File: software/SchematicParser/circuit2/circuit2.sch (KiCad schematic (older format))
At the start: 8 parts, among them Q1 Transistor, U1-8 8pinChip

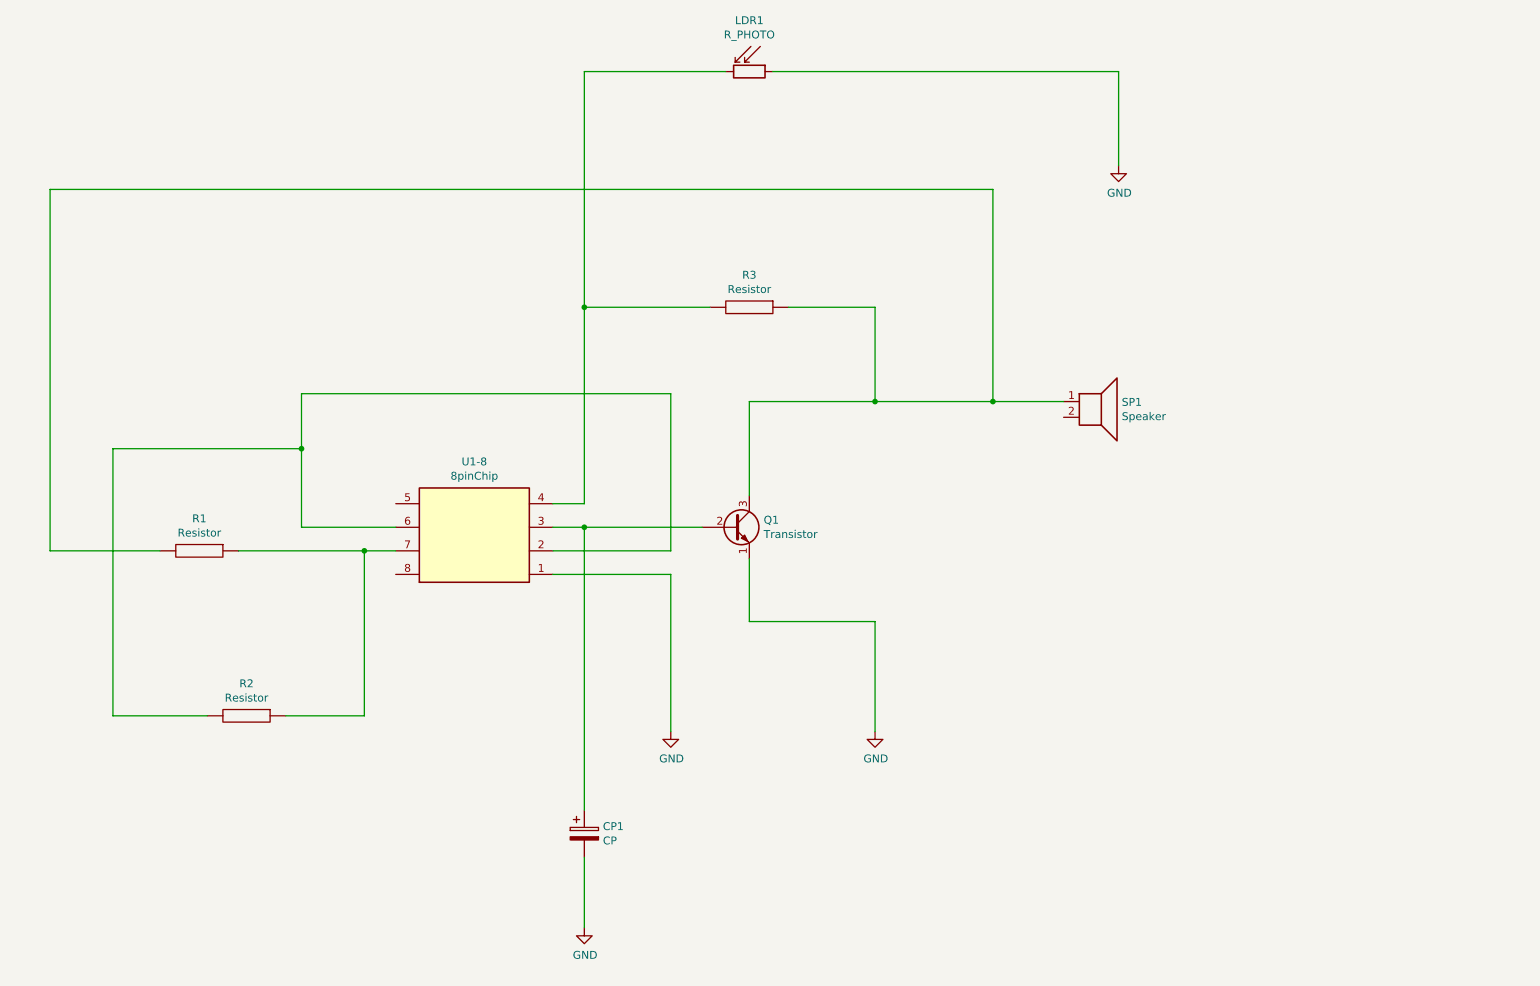
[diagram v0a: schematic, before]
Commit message: modify scale of prefabs
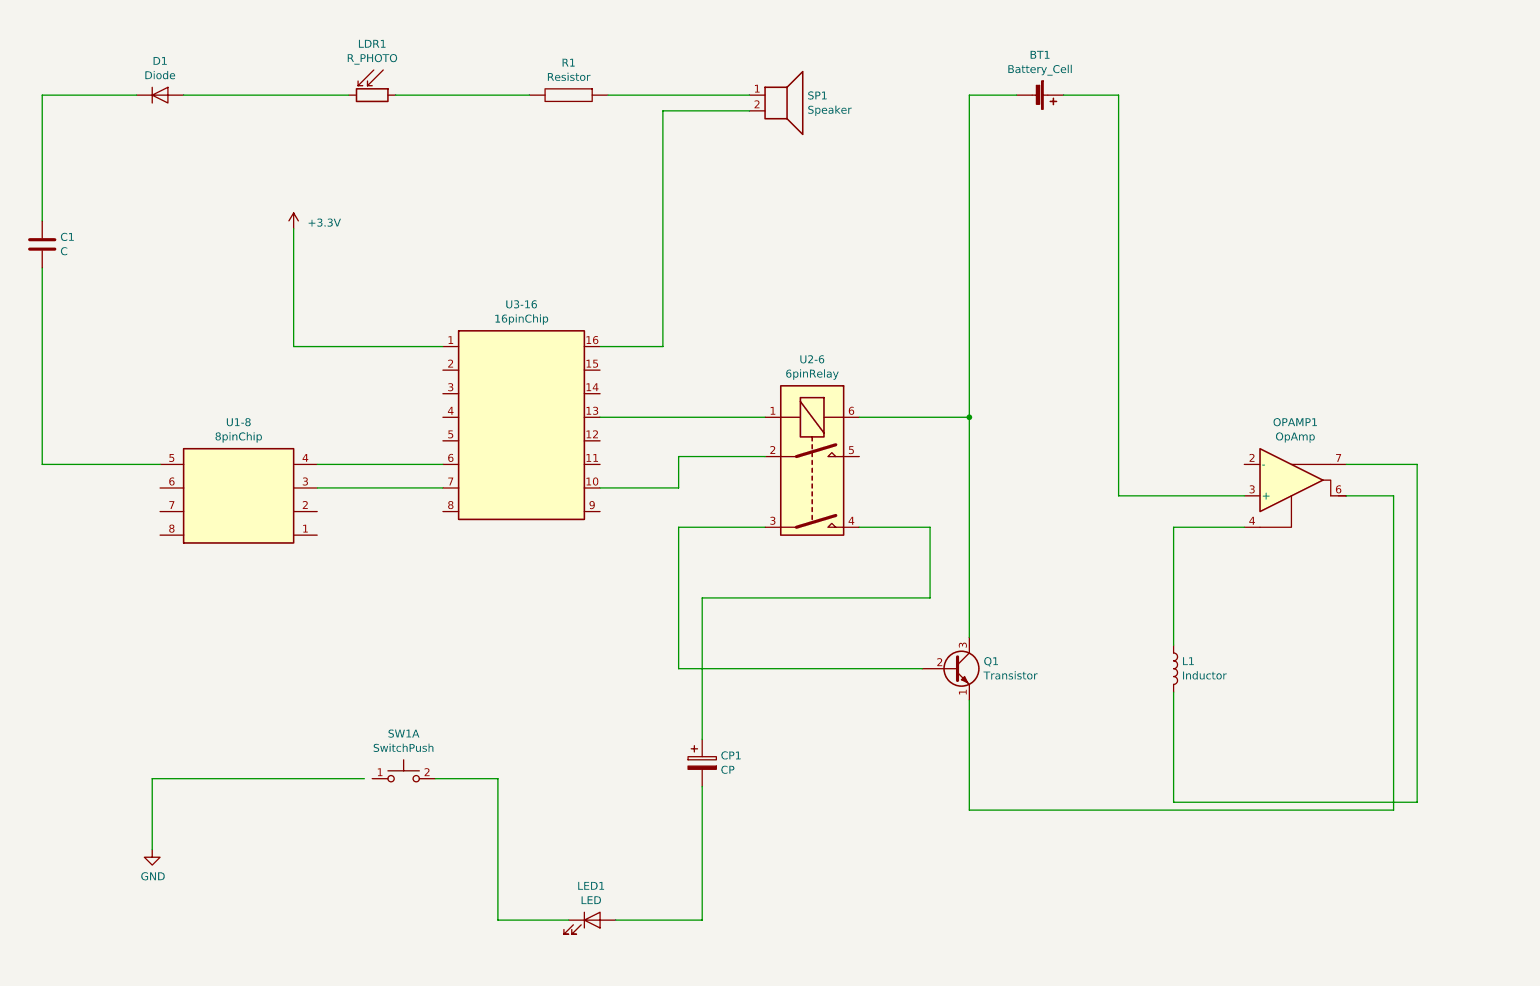
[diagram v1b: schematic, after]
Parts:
- removed R1, R2: Resistor, symbol SchemaBoard_Library:Resistor
- added BT1: Battery_Cell, symbol SchemaBoard_Library:Battery_Cell
- added C1: C, symbol SchemaBoard_Library:C
- added D1: Diode, symbol SchemaBoard_Library:Diode
- added GND1: GND, symbol SchemaBoard_Library:GND
- added L1: Inductor, symbol SchemaBoard_Library:Inductor
- added LED1: LED, symbol SchemaBoard_Library:LED
- added OPAMP1: OpAmp, symbol SchemaBoard_Library:OpAmp
- added PWR1: +3.3V, symbol SchemaBoard_Library:+3.3V
- added SW1: SwitchPush, symbol SchemaBoard_Library:SwitchPush
- added U2-6: 6pinRelay, Relay_THT, symbol SchemaBoard_Library:6pinRelay
- added U3-16: 16pinChip, symbol SchemaBoard_Library:16pinChip
- renumbered R3 to R1
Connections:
- net GND: now also GND1.1 (GND); no longer CP1.2, LDR1.1, Q1.1 (E), U1-8.1
- net at U1-8.2: no longer U1-8.6
- net at U1-8.5: now also C1.2
- net at R1.1, SP1.1: no longer Q1.3 (C)
- net at SP1.2: now also U3-16.16
- new net: U1-8.3, U3-16.7
- new net: U1-8.4, U3-16.6
- new net: LDR1.1, R1.2
- new net: D1.2 (A), LDR1.2
- new net: OPAMP1.6, Q1.1 (E)
- new net: Q1.2 (B), U2-6.3
- new net: BT1.2 (-), Q1.3 (C), U2-6.6
- new net: U2-6.1, U3-16.13
- new net: U2-6.2, U3-16.10
- new net: CP1.1, U2-6.4
- new net: C1.1, D1.1 (K)
- new net: L1.1, OPAMP1.4
- new net: L1.2, OPAMP1.7
- new net: LED1.1 (K), SW1.2 (D)
- new net: CP1.2, LED1.2 (A)
- new net: BT1.1 (+), OPAMP1.3 (+)
- new net +3V3: PWR1.1 (+3V3), U3-16.1
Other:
- moved on the sheet: CP1, LDR1, Q1, R1, SP1, U1-8

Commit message: Bugfix solved the touch problem of profabs
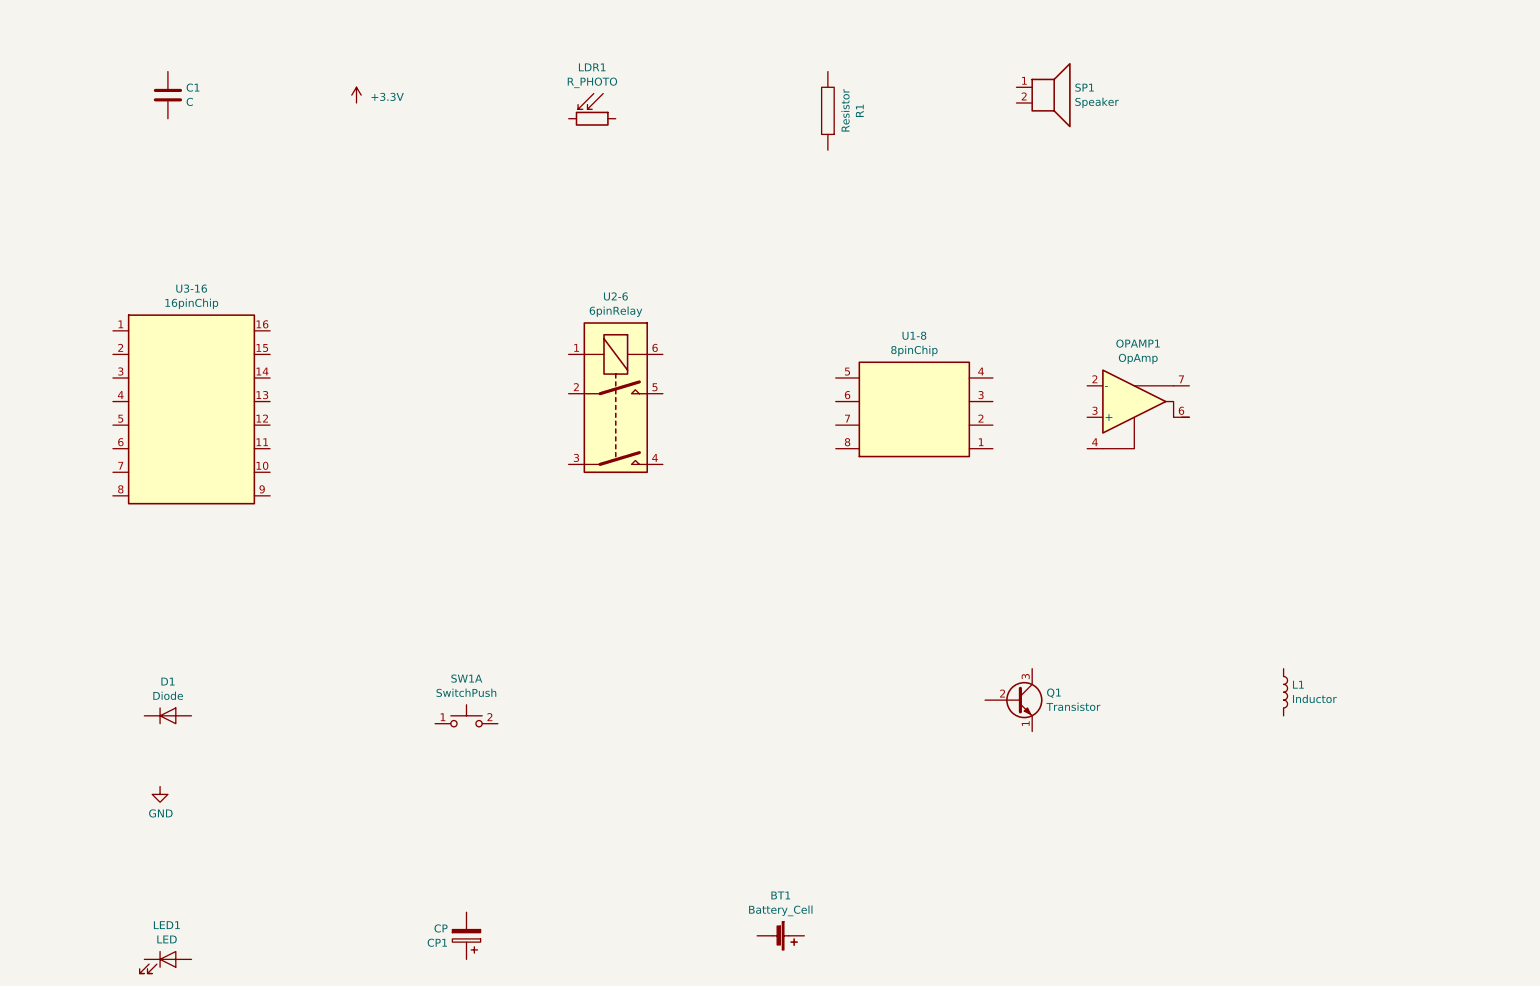
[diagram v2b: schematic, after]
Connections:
- net +3V3: no longer U3-16.1
- net at U1-8.3: no longer U3-16.7
- net at U1-8.4: no longer U3-16.6
- net at U1-8.5: no longer C1.2
- net at SP1.1: no longer R1.1
- net at SP1.2: no longer U3-16.16
- net at LDR1.1: no longer R1.2
- net at LDR1.2: no longer D1.2 (A)
- net at Q1.1 (E): no longer OPAMP1.6
- net at Q1.2 (B): no longer U2-6.3
- net at U2-6.1: no longer U3-16.13
- net at U2-6.2: no longer U3-16.10
- net at U2-6.4: no longer CP1.1
- net at C1.1: no longer D1.1 (K)
- net at L1.1: no longer OPAMP1.4
- net at L1.2: no longer OPAMP1.7
- net at LED1.1 (K): no longer SW1.2 (D)
- net at LED1.2 (A): no longer CP1.2
- net at OPAMP1.3 (+): no longer BT1.1 (+)
- now unconnected: BT1.2 (-), Q1.3 (C), U2-6.6
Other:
- moved on the sheet: BT1, C1, CP1, D1, L1, LDR1, LED1, OPAMP1, Q1, R1, SP1, SW1A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

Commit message: Bugfix remove space when split string into string[]
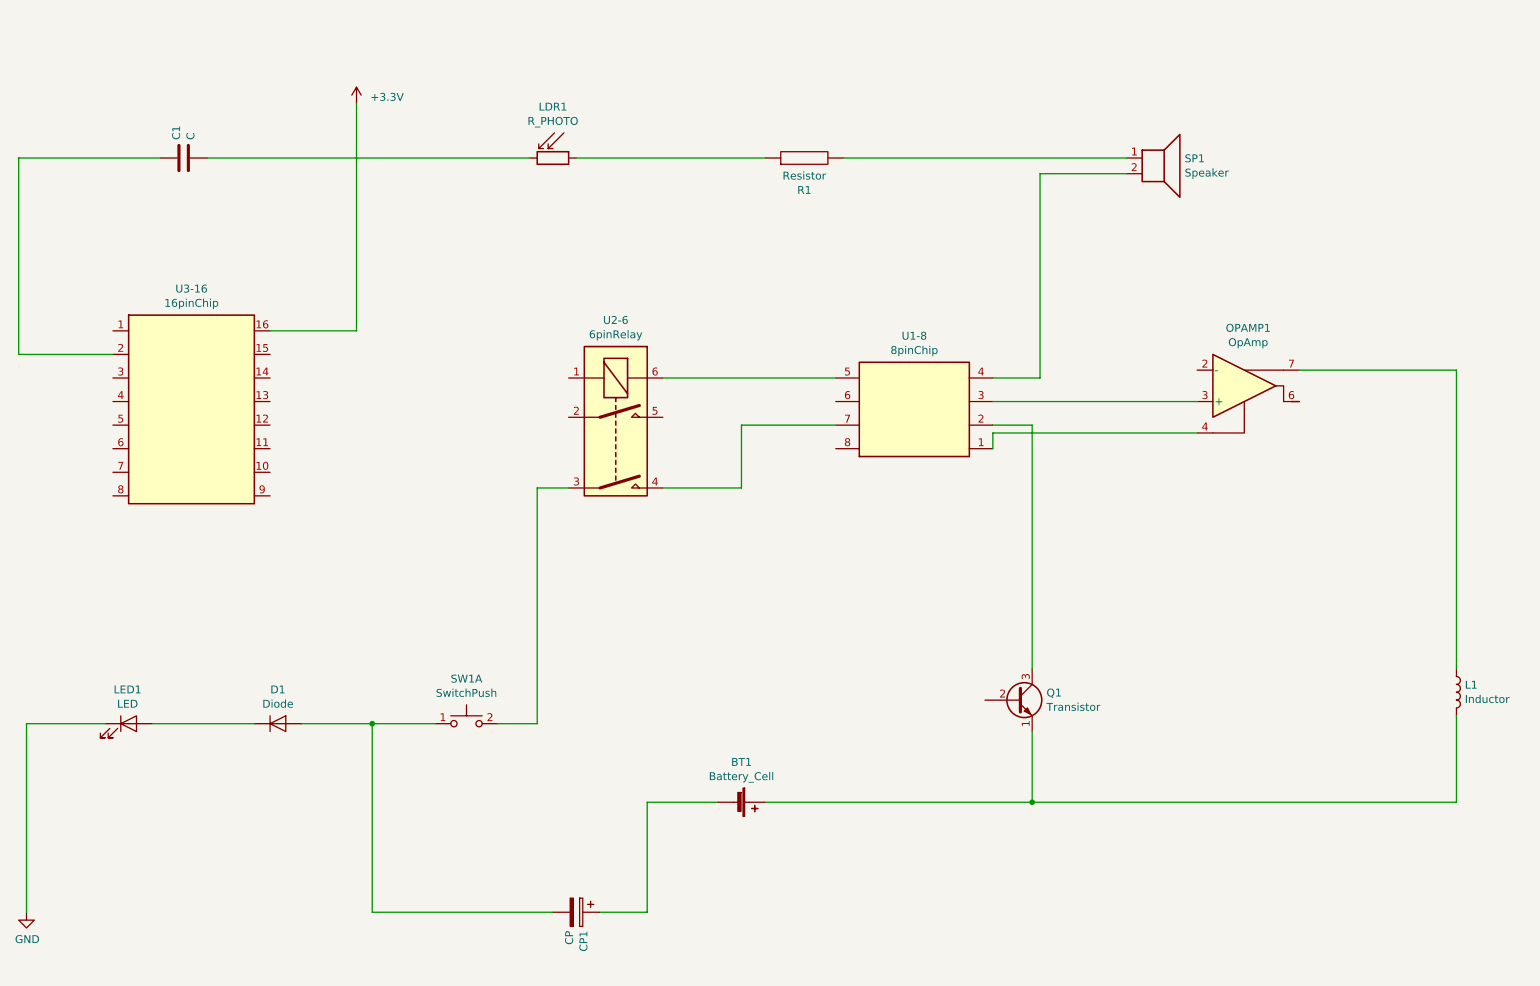
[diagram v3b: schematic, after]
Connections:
- net +3V3: now also U3-16.16
- net GND: now also LED1.1 (K)
- net at U1-8.1: now also OPAMP1.4
- net at U1-8.2: now also Q1.3 (C)
- net at U1-8.3: now also OPAMP1.3 (+)
- net at U1-8.4: now also SP1.2
- net at U1-8.5: now also U2-6.6
- net at U1-8.7: now also U2-6.4
- net at SP1.1: now also R1.2
- net at LDR1.1: now also R1.1
- net at LDR1.2: now also C1.2
- net at Q1.1 (E): now also BT1.1 (+), L1.2
- net at U2-6.3: now also SW1.2 (D)
- net at U3-16.2: now also C1.1
- net at D1.1 (K): now also LED1.2 (A)
- net at D1.2 (A): now also CP1.2, SW1.1 (C)
- net at L1.1: now also OPAMP1.7
- net at BT1.2 (-): now also CP1.1
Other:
- moved on the sheet: BT1, C1, CP1, D1, L1, LDR1, LED1, OPAMP1, R1, SP1, U2-6
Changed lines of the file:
@@
 L SchemaBoard_Library:C C1
 U 1 1 5D3E4A94
-P 1850 1650
-F 0 "C1" H 1965 1696 50  0000 L CNN
-F 1 "C" H 1965 1605 50  0000 L CNN
-F 2 "" H 1888 1500 50  0001 C CNN
-F 3 "~" H 1850 1650 50  0001 C CNN
-	1    1850 1650
-	1    0    0    -1
+P 1950 2050
+F 0 "C1" H 2065 2096 50  0000 L CNN
+F 1 "C" H 2065 2005 50  0000 L CNN
+F 2 "" H 1988 1900 50  0001 C CNN
+F 3 "~" H 1950 2050 50  0001 C CNN
+	1    1950 2050
+	0    -1   -1   0
 $EndComp
 $Comp
@@
 L SchemaBoard_Library:R_PHOTO LDR1
 U 1 1 5D3CE114
-P 4550 1800
-F 0 "LDR1" V 4225 1800 50  0000 C CNN
-F 1 "R_PHOTO" V 4316 1800 50  0000 C CNN
-F 2 "" V 4600 1550 50  0001 L CNN
-F 3 "~" H 4550 1750 50  0001 C CNN
-	1    4550 1800
+P 4300 2050
+F 0 "LDR1" V 3975 2050 50  0000 C CNN
+F 1 "R_PHOTO" V 4066 2050 50  0000 C CNN
+F 2 "" V 4350 1800 50  0001 L CNN
+F 3 "~" H 4300 2000 50  0001 C CNN
+	1    4300 2050
 	0    1    1    0
 $EndComp
@@
 L SchemaBoard_Library:Resistor R1
 U 1 1 5D3CF2F7
-P 6050 1750
-F 0 "R1" V 5845 1750 50  0000 C CNN
-F 1 "Resistor" V 5936 1750 50  0000 C CNN
-F 2 "" H 6050 1750 50  0001 C CNN
-F 3 "~" H 6050 1750 50  0001 C CNN
-	1    6050 1750
-	-1   0    0    1
+P 5900 2050
+F 0 "R1" V 5695 2050 50  0000 C CNN
+F 1 "Resistor" V 5786 2050 50  0000 C CNN
+F 2 "" H 5900 2050 50  0001 C CNN
+F 3 "~" H 5900 2050 50  0001 C CNN
+	1    5900 2050
+	0    -1   -1   0
 $EndComp
 $Comp
 L SchemaBoard_Library:Speaker SP1
 U 1 1 5D3CD94C
-P 7450 1600
-F 0 "SP1" H 7620 1596 50  0000 L CNN
-F 1 "Speaker" H 7620 1505 50  0000 L CNN
-F 2 "" H 7450 1400 50  0001 C CNN
-F 3 "~" H 7440 1550 50  0001 C CNN
-	1    7450 1600
+P 8150 2050
+F 0 "SP1" H 8320 2046 50  0000 L CNN
+F 1 "Speaker" H 8320 1955 50  0000 L CNN
+F 2 "" H 8150 1850 50  0001 C CNN
+F 3 "~" H 8140 2000 50  0001 C CNN
+	1    8150 2050
 	1    0    0    -1
 $EndComp
@@
 L SchemaBoard_Library:OpAmp OPAMP1
 U 1 1 5D3E6608
-P 8000 3600
-F 0 "OPAMP1" H 8025 3967 50  0000 C CNN
-F 1 "OpAmp" H 8025 3876 50  0000 C CNN
-F 2 "" H 8000 3600 50  0001 C CNN
-F 3 "~" H 8000 3600 50  0001 C CNN
-	1    8000 3600
+P 8700 3500
+F 0 "OPAMP1" H 8725 3867 50  0000 C CNN
+F 1 "OpAmp" H 8725 3776 50  0000 C CNN
+F 2 "" H 8700 3500 50  0001 C CNN
+F 3 "~" H 8700 3500 50  0001 C CNN
+	1    8700 3500
 	1    0    0    -1
 $EndComp
@@
 L SchemaBoard_Library:6pinRelay U2-6
 U 1 1 5D3E2F18
-P 4700 3600
-F 0 "U2-6" V 4033 3600 50  0000 C CNN
-F 1 "6pinRelay" V 4124 3600 50  0000 C CNN
-F 2 "Relay_THT" H 5200 3500 50  0001 L CNN
-F 3 "https://standexelectronics.com/wp-content/uploads/datasheet_reed_relay_DIP.pdf" H 4600 3600 50  0001 C CNN
-	1    4700 3600
+P 4700 3750
+F 0 "U2-6" V 4033 3750 50  0000 C CNN
+F 1 "6pinRelay" V 4124 3750 50  0000 C CNN
+F 2 "Relay_THT" H 5200 3650 50  0001 L CNN
+F 3 "https://standexelectronics.com/wp-content/uploads/datasheet_reed_relay_DIP.pdf" H 4600 3750 50  0001 C CNN
+	1    4700 3750
 	0    1    1    0
 $EndComp
@@
 L SchemaBoard_Library:Diode D1
 U 1 1 5D3E50B4
-P 1850 5600
-F 0 "D1" H 1850 5816 50  0000 C CNN
-F 1 "Diode" H 1850 5725 50  0000 C CNN
-F 2 "" H 1850 5600 50  0001 C CNN
-F 3 "~" H 1850 5600 50  0001 C CNN
-	1    1850 5600
+P 2550 5650
+F 0 "D1" H 2550 5866 50  0000 C CNN
+F 1 "Diode" H 2550 5775 50  0000 C CNN
+F 2 "" H 2550 5650 50  0001 C CNN
+F 3 "~" H 2550 5650 50  0001 C CNN
+	1    2550 5650
 	1    0    0    -1
 $EndComp
@@
 L SchemaBoard_Library:CP CP1
 U 1 1 5D3FE055
-P 3750 7000
-F 0 "CP1" H 3868 7046 50  0000 L CNN
-F 1 "CP" H 3868 6955 50  0000 L CNN
-F 2 "" H 3788 6850 50  0001 C CNN
-F 3 "~" H 3750 7000 50  0001 C CNN
-	1    3750 7000
-	-1   0    0    1
+P 4450 6850
+F 0 "CP1" H 4568 6896 50  0000 L CNN
+F 1 "CP" H 4568 6805 50  0000 L CNN
+F 2 "" H 4488 6700 50  0001 C CNN
+F 3 "~" H 4450 6850 50  0001 C CNN
+	1    4450 6850
+	0    1    1    0
 $EndComp
 $Comp
@@
 L SchemaBoard_Library:Inductor L1
 U 1 1 5D3E5584
-P 8950 5450
-F 0 "L1" H 9003 5496 50  0000 L CNN
-F 1 "Inductor" H 9003 5405 50  0000 L CNN
-F 2 "" H 8950 5450 50  0001 C CNN
-F 3 "~" H 8950 5450 50  0001 C CNN
-	1    8950 5450
+P 10050 5450
+F 0 "L1" H 10103 5496 50  0000 L CNN
+F 1 "Inductor" H 10103 5405 50  0000 L CNN
+F 2 "" H 10050 5450 50  0001 C CNN
+F 3 "~" H 10050 5450 50  0001 C CNN
+	1    10050 5450
 	1    0    0    -1
 $EndComp
@@
 L SchemaBoard_Library:GND GND1
 U 1 1 5D3D0965
-P 1800 6050
-F 0 "GND1" H 1800 5800 50  0001 C CNN
-F 1 "GND" H 1805 5877 50  0000 C CNN
-F 2 "" H 1800 6050 50  0001 C CNN
-F 3 "" H 1800 6050 50  0001 C CNN
-	1    1800 6050
+P 950 6850
+F 0 "GND1" H 950 6600 50  0001 C CNN
+F 1 "GND" H 955 6677 50  0000 C CNN
+F 2 "" H 950 6850 50  0001 C CNN
+F 3 "" H 950 6850 50  0001 C CNN
+	1    950  6850
 	1    0    0    -1
 $EndComp
@@
 L SchemaBoard_Library:LED LED1
 U 1 1 5D3E5DAB
-P 1850 7150
-F 0 "LED1" H 1843 7366 50  0000 C CNN
-F 1 "LED" H 1843 7275 50  0000 C CNN
-F 2 "" H 1850 7150 50  0001 C CNN
-F 3 "~" H 1850 7150 50  0001 C CNN
-	1    1850 7150
+P 1600 5650
+F 0 "LED1" H 1593 5866 50  0000 C CNN
+F 1 "LED" H 1593 5775 50  0000 C CNN
+F 2 "" H 1600 5650 50  0001 C CNN
+F 3 "~" H 1600 5650 50  0001 C CNN
+	1    1600 5650
 	1    0    0    -1
 $EndComp
@@
 L SchemaBoard_Library:Battery_Cell BT1
 U 1 1 5D3EC35E
-P 5700 7000
-F 0 "BT1" V 5445 7050 50  0000 C CNN
-F 1 "Battery_Cell" V 5536 7050 50  0000 C CNN
-F 2 "" V 5700 7060 50  0001 C CNN
-F 3 "~" V 5700 7060 50  0001 C CNN
-	1    5700 7000
-	0    1    1    0
-$EndComp
+P 5450 6150
+F 0 "BT1" V 5195 6200 50  0000 C CNN
+F 1 "Battery_Cell" V 5286 6200 50  0000 C CNN
+F 2 "" V 5450 6210 50  0001 C CNN
+F 3 "~" V 5450 6210 50  0001 C CNN
+	1    5450 6150
+	0    1    1    0
+$EndComp
+Wire Wire Line
+	3050 1700 3050 3150
+Wire Wire Line
+	3050 3150 2500 3150
+Wire Wire Line
+	2100 2050 4150 2050
+Wire Wire Line
+	4450 2050 5650 2050
+Wire Wire Line
+	1800 2050 900  2050
+Wire Wire Line
+	900  2050 900  3300
+Wire Wire Line
+	900  3300 1500 3300
+Wire Wire Line
+	6150 2050 7950 2050
+Wire Wire Line
+	7950 2150 7400 2150
+Wire Wire Line
+	7400 2150 7400 3450
+Wire Wire Line
+	7400 3450 7100 3450
+Wire Wire Line
+	7100 3600 8400 3600
+Wire Wire Line
+	9050 3400 10050 3400
+Wire Wire Line
+	10050 3400 10050 5300
+Wire Wire Line
+	10050 5600 10050 6150
+Wire Wire Line
+	10050 6150 7350 6150
+Wire Wire Line
+	7350 6150 7350 5700
+Wire Wire Line
+	7100 3750 7350 3750
+Wire Wire Line
+	7350 3750 7350 5300
+Wire Wire Line
+	5000 3450 6100 3450
+Wire Wire Line
+	6100 3750 5500 3750
+Wire Wire Line
+	5500 3750 5500 4150
+Wire Wire Line
+	5500 4150 5000 4150
+Wire Wire Line
+	4400 4150 4200 4150
+Wire Wire Line
+	4200 4150 4200 5650
+Wire Wire Line
+	4200 5650 3950 5650
+Wire Wire Line
+	8400 3800 7100 3800
+Wire Wire Line
+	7100 3800 7100 3900
+Wire Wire Line
+	2700 5650 3150 5650
+Wire Wire Line
+	1750 5650 2400 5650
+Wire Wire Line
+	5650 6150 7350 6150
+Connection ~ 7350 6150
+Wire Wire Line
+	5350 6150 4900 6150
+Wire Wire Line
+	4900 6150 4900 6850
+Wire Wire Line
+	4900 6850 4600 6850
+Wire Wire Line
+	4300 6850 3150 6850
+Wire Wire Line
+	3150 6850 3150 5650
+Connection ~ 3150 5650
+Wire Wire Line
+	3150 5650 3550 5650
+Wire Wire Line
+	1450 5650 950  5650
+Wire Wire Line
+	950  5650 950  6850
 $EndSCHEMATC
